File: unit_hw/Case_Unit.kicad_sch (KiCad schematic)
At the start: 15 parts, among them J1 Conn_01x02, J2 Conn_01x04, J3 RJ45, J4 Conn_01x03, Q1 2N7002, U1 SPX3819M5-L-3-3, U2 STM32G030F6Px, U3 MAX487E

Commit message: Revise unit schematic
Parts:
- removed J1: Conn_01x02, Connector_PinHeader_2.54mm:PinHeader_1x02_P2.54mm_Vertical, symbol Connector_Generic:Conn_01x02
- removed Q1: 2N7002, Package_TO_SOT_SMD:SOT-23, symbol Device:Q_NMOS_GSD
- removed U1: SPX3819M5-L-3-3, Package_TO_SOT_SMD:SOT-23-5, symbol Regulator_Linear:SPX3819M5-L-3-3
- removed U2: STM32G030F6Px, Package_SO:TSSOP-20_4.4x6.5mm_P0.65mm, symbol MCU_ST_STM32G0:STM32G030F6Px
- added C3, C4: 22u, Capacitor_SMD:C_0603_1608Metric, symbol Device:C
- added C5: 100n, Capacitor_SMD:C_0402_1005Metric, symbol Device:C
- added L1: 10u, Inductor_SMD:L_Changjiang_FNR5030S, symbol Device:L
- added R2: 100k, Resistor_SMD:R_0402_1005Metric, symbol Device:R
- added R3: 13k, Resistor_SMD:R_0402_1005Metric, symbol Device:R
- added U1: MT2492, Package_TO_SOT_SMD:SOT-23-6, symbol MT2492:MT2492
- added U2: PY32F003F18U6, Package_DFN_QFN:QFN-20-1EP_3x3mm_P0.4mm_EP1.65x1.65mm, symbol Case_symbols:PY32F003F18U6TR
- C1: value 4.7u -> 100n; footprint Capacitor_SMD:C_0402_1005Metric -> Capacitor_SMD:C_0603_1608Metric
- C2: value 10n -> 22u; footprint Capacitor_SMD:C_0402_1005Metric -> Capacitor_SMD:C_0603_1608Metric
- R1: value 4.7k -> 1; footprint Resistor_SMD:R_0402_1005Metric -> (none)
- renumbered C3 to C6, C4 to C7, J2 to J1, R3 to R4, R2 to R5
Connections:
- net MAX487_RE is gone; now on net MAX487_DE: U3.2 (~{RE})
- net +5V: now also C6.1, J1.1 (Pin_1), C3.1, C4.1, L1.2, R2.1, U2.6 (VCC); no longer R1.1
- net GND: now also J3.2, C3.2, C4.2, R3.2, U1.2 (GND), U2.21 (PAD), U2.4 (VSS)
- net MAX487_DE: now also U2.20 (PA4)
- net SERVO_OUT: now also U2.16 (PA0); no longer R1.2
- net SWCLK: now also U2.8 (PA14)
- net SWDIO: now also U2.7 (PA13)
- net UART_RX: now also U2.19 (PA3)
- net UART_TX: now also U2.18 (PA2)
- net at C2.1: now also R1.2, U1.4 (EN), U1.5 (IN)
- net VIN: now reaches J3.1
- net VIN: now also C1.1, R1.1
- removed net +3V3: C1.1, C6.1, J1.1 (Pin_1)
- new net: C5.1, U1.1 (BS)
- new net: R2.2, R3.1, U1.3 (FB)
- new net: C5.2, L1.1, U1.6 (SW)
- no-connect marks 17 -> 16
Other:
- note added: "(130k)"
- note added: "(20k)"
- note added: "Consider MP2359"
- note added: "FB ref. 0.6 V typ. (0.8 V MP2359)"
- note added: "PA0 AF13 TIM1_CH3"
- note added: "PA2 AF1 USART1_TX"
- note added: "PA3 AF1 USART1_RX"
- note added: "Set output = 5.2 V"
- note removed: "PA2 AF1 USART2_TX"
- note removed: "PA3 AF1 USART2_RX FT_ea"
- note removed: "PA7 AF5 TIM17_CH1"
- moved on the sheet: C6

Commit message: Submit for fab (Rev. 2 unit)
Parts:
- C1: footprint Capacitor_SMD:C_0603_1608Metric -> Capacitor_SMD:C_0402_1005Metric
- R1: footprint (none) -> Resistor_SMD:R_0402_1005Metric
- renumbered J3 to J2, J4 to J3
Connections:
- net GND: now also J2.3, J2.4, J2.5, J2.6
- net MAX487_DE: now also U2.17 (PA1); no longer U2.20 (PA4)
- net SERVO_OUT: now also U2.3 (PA7); no longer U2.16 (PA0)
- no-connect marks 16 -> 12
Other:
- note added: "PA7 AF2 TIM1_CH1N"
- note removed: "PA0 AF13 TIM1_CH3"
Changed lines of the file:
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@@
   (junction (at -6.35 43.815) (diameter 0) (color 0 0 0 0)
   )
+  (junction (at 4.445 109.855) (diameter 0) (color 0 0 0 0)
+  )
   (junction (at -6.35 51.435) (diameter 0) (color 0 0 0 0)
   )
   (junction (at 127.635 106.68) (diameter 0) (color 0 0 0 0)
   )
+  (junction (at 4.445 114.935) (diameter 0) (color 0 0 0 0)
+  )
   (junction (at 104.14 111.76) (diameter 0) (color 0 0 0 0)
   )
+  (junction (at 4.445 112.395) (diameter 0) (color 0 0 0 0)
+  )
   (junction (at -45.72 36.195) (diameter 0) (color 0 0 0 0)
   )
   (junction (at -17.78 36.195) (diameter 0) (color 0 0 0 0)
+  )
+  (junction (at 4.445 116.84) (diameter 0) (color 0 0 0 0)
   )
   (junction (at 6.985 116.84) (diameter 0) (color 0 0 0 0)
@@
   (no_connect (at 71.12 67.945))
   (no_connect (at 68.58 67.945))
-  (no_connect (at 52.705 55.245))
-  (no_connect (at 4.445 112.395))
-  (no_connect (at 4.445 109.855))
+  (no_connect (at 71.12 41.91))
   (no_connect (at 52.705 52.705))
   (no_connect (at 52.705 60.325))
-  (no_connect (at 4.445 107.315))
+  (no_connect (at 60.96 41.91))
   (no_connect (at 78.74 55.245))
   (no_connect (at 78.74 60.325))
   (no_connect (at 52.705 50.165))
   (no_connect (at 78.74 57.785))
-  (no_connect (at 4.445 114.935))
-  (no_connect (at 68.58 41.91))
   (no_connect (at 78.74 50.165))
+  (wire (pts (xy 4.445 114.935) (xy 4.445 116.84))
+    (stroke (width 0) (type default))
+  )
   (wire (pts (xy 50.165 56.515) (xy 52.705 56.515))
     (stroke (width 0) (type default))
@@
     (stroke (width 0) (type default))
   )
-  (wire (pts (xy 60.96 39.37) (xy 60.96 41.91))
+  (wire (pts (xy 68.58 39.37) (xy 68.58 41.91))
     (stroke (width 0) (type default))
   )
@@
     (stroke (width 0) (type default))
   )
+  (wire (pts (xy 4.445 109.855) (xy 4.445 112.395))
+    (stroke (width 0) (type default))
+  )
   (wire (pts (xy 6.35 104.775) (xy 4.445 104.775))
     (stroke (width 0) (type default))
@@
     (stroke (width 0) (type default))
   )
-  (wire (pts (xy 71.12 39.37) (xy 71.12 41.91))
+  (wire (pts (xy 50.165 55.245) (xy 52.705 55.245))
     (stroke (width 0) (type default))
   )
@@
     (stroke (width 0) (type default))
   )
+  (wire (pts (xy 4.445 107.315) (xy 4.445 109.855))
+    (stroke (width 0) (type default))
+  )
   (wire (pts (xy 51.435 67.945) (xy 60.96 67.945))
     (stroke (width 0) (type default))
@@
   )
   (wire (pts (xy 66.04 39.37) (xy 66.04 41.91))
+    (stroke (width 0) (type default))
+  )
+  (wire (pts (xy 4.445 112.395) (xy 4.445 114.935))
     (stroke (width 0) (type default))
   )
@@
     (effects (font (size 1.27 1.27) italic) (justify left bottom))
   )
-  (text "PA0 AF13 TIM1_CH3" (at 72.39 31.75 0)
-    (effects (font (size 1.27 1.27) italic) (justify left bottom))
+  (text "PA7 AF2 TIM1_CH1N" (at 50.165 52.705 0)
+    (effects (font (size 1.27 1.27) italic) (justify right bottom))
   )
   (text "(20k)" (at -4.445 49.53 0)
@@
     (effects (font (size 1.27 1.27)) (justify right bottom))
   )
-  (label "SERVO_OUT" (at 71.12 39.37 90) (fields_autoplaced)
-    (effects (font (size 1.27 1.27)) (justify left bottom))
+  (label "SERVO_OUT" (at 50.165 55.245 180) (fields_autoplaced)
+    (effects (font (size 1.27 1.27)) (justify right bottom))
   )
   (label "RS422-" (at 6.35 102.235 0) (fields_autoplaced)
     (effects (font (size 1.27 1.27)) (justify left bottom))
   )
-  (label "MAX487_DE" (at 60.96 39.37 90) (fields_autoplaced)
+  (label "MAX487_DE" (at 68.58 39.37 90) (fields_autoplaced)
     (effects (font (size 1.27 1.27)) (justify left bottom))
   )
@@
       (effects (font (size 1.27 1.27)))
     )
-    (property "Footprint" "" (at -58.42 37.973 90)
+    (property "Footprint" "Resistor_SMD:R_0402_1005Metric" (at -58.42 37.973 90)
       (effects (font (size 1.27 1.27)) hide)
     )
@@
       (effects (font (size 1.27 1.27)) (justify left))
     )
-    (property "Footprint" "Capacitor_SMD:C_0603_1608Metric" (at -67.0052 43.815 0)
+    (property "Footprint" "Capacitor_SMD:C_0402_1005Metric" (at -67.0052 43.815 0)
       (effects (font (size 1.27 1.27)) hide)
     )
@@
   (symbol (lib_id "Connector_Generic:Conn_01x03") (at -11.43 133.35 0) (unit 1)
     (in_bom yes) (on_board yes) (dnp no)
-    (property "Reference" "J4" (at -8.89 133.35 0)
+    (property "Reference" "J3" (at -8.89 133.35 0)
       (effects (font (size 1.27 1.27)) (justify left))
     )
@@
       (project "Case_Unit"
         (path "/29c85a4f-01dc-47ac-a552-a3c6d1f580bd"
-          (reference "J4") (unit 1)
+          (reference "J3") (unit 1)
         )
       )
@@
   (symbol (lib_id "Connector:RJ45") (at -5.715 112.395 0) (unit 1)
     (in_bom yes) (on_board yes) (dnp no) (fields_autoplaced)
-    (property "Reference" "J3" (at -5.715 95.25 0)
+    (property "Reference" "J2" (at -5.715 95.25 0)
       (effects (font (size 1.27 1.27)))
     )
@@
       (project "Case_Unit"
         (path "/29c85a4f-01dc-47ac-a552-a3c6d1f580bd"
-          (reference "J3") (unit 1)
-        )
-      )
+          (reference "J2") (unit 1)
+        )
+      )

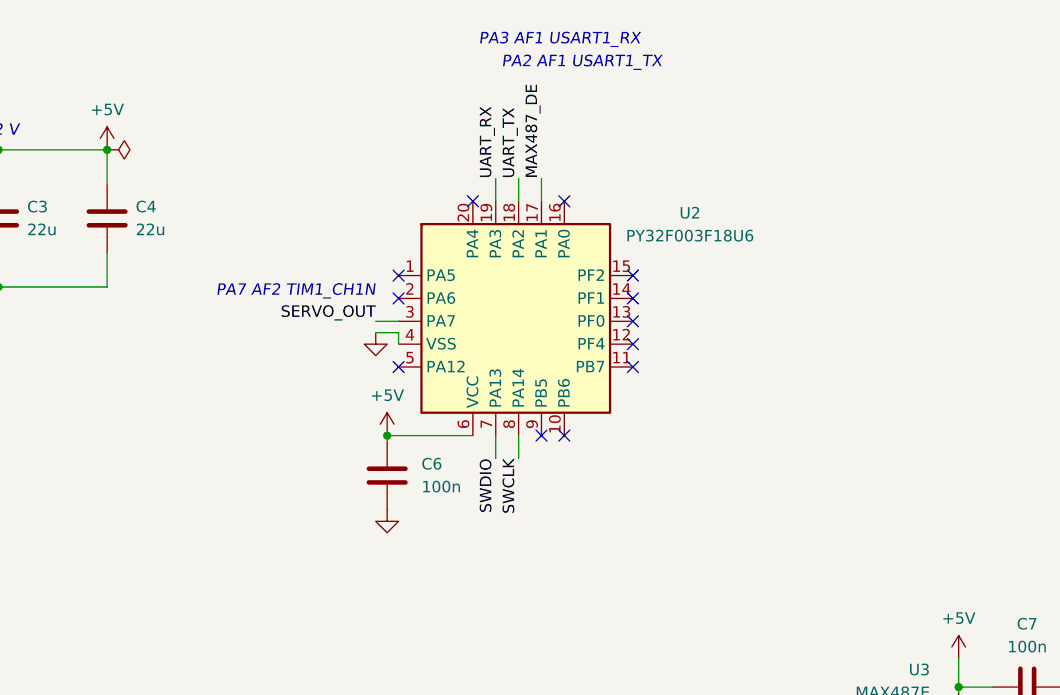
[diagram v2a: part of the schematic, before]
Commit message: Revise unit board (change PY32 model to 002B; add crystal)
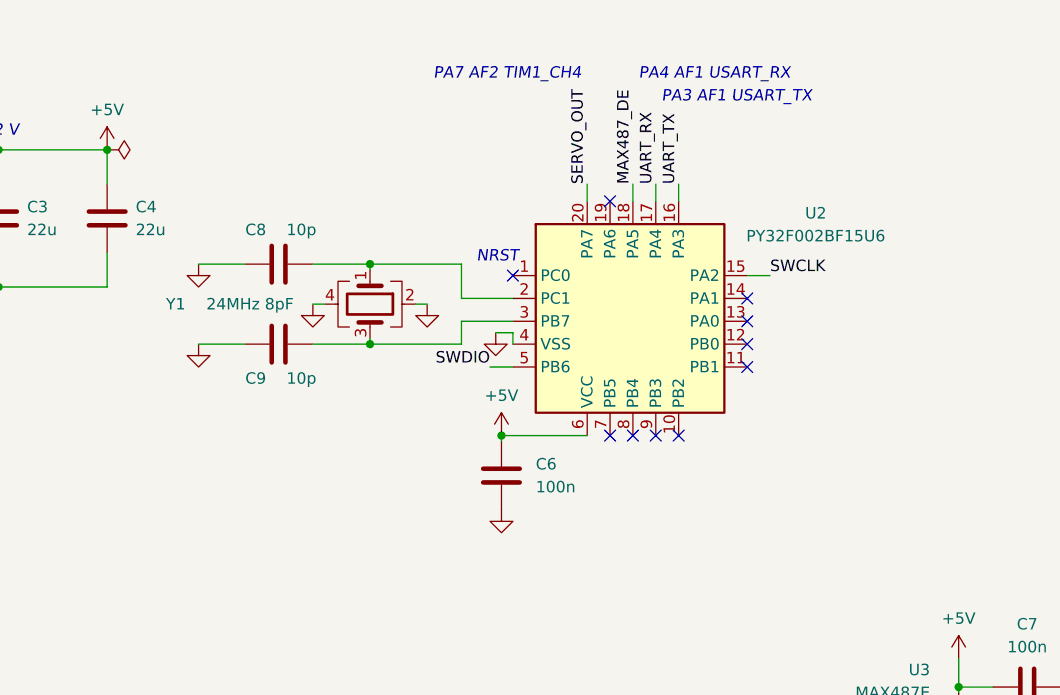
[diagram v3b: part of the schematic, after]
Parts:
- removed U2: PY32F003F18U6, Package_DFN_QFN:QFN-20-1EP_3x3mm_P0.4mm_EP1.65x1.65mm, symbol Case_symbols:PY32F003F18U6TR
- added C8, C9: 10p, Capacitor_SMD:C_0402_1005Metric, symbol Device:C
- added U2: PY32F002BF15U6, Package_DFN_QFN:QFN-20-1EP_3x3mm_P0.4mm_EP1.65x1.65mm, symbol Case_symbols:PY32F002BF15U6TR
- added Y1: 24MHz 8pF, Crystal:Crystal_SMD_2016-4Pin_2.0x1.6mm, symbol Device:Crystal_GND24
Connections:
- net +5V: now also U2.6 (VCC)
- net GND: now also C8.1, C9.1, U2.21 (PAD), U2.4 (VSS), Y1.2, Y1.4
- net MAX487_DE: now also U2.18 (PA5)
- net SERVO_OUT: now also U2.20 (PA7)
- net SWCLK: now also U2.15 (PA2)
- net SWDIO: now also U2.5 (PB6)
- net UART_RX: now also U2.17 (PA4)
- net UART_TX: now also U2.16 (PA3)
- new net: C8.2, U2.2 (PC1), Y1.1
- new net: C9.2, U2.3 (PB7), Y1.3
- no-connect marks 12 -> 10
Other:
- note added: "NRST"
- note added: "PA3 AF1 USART_TX"
- note added: "PA4 AF1 USART_RX"
- note added: "PA7 AF2 TIM1_CH4"
- note removed: "PA2 AF1 USART1_TX"
- note removed: "PA3 AF1 USART1_RX"
- note removed: "PA7 AF2 TIM1_CH1N"
- moved on the sheet: C6

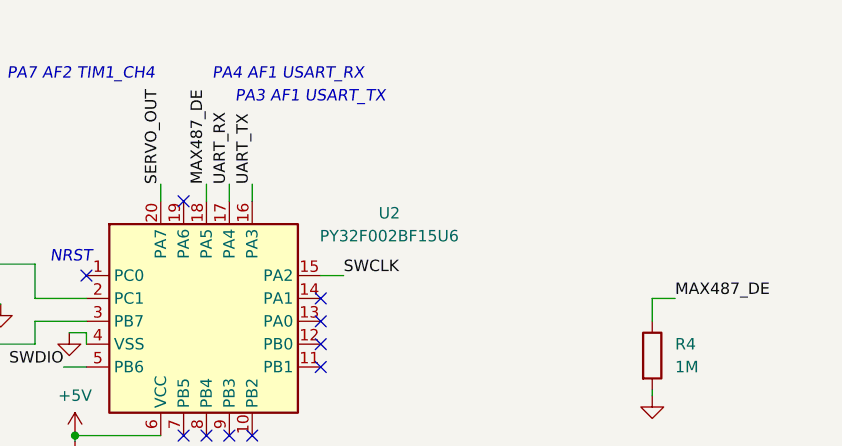
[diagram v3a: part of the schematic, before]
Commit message: Finish unit redesign; submit for fab (Rev. 2 unit)
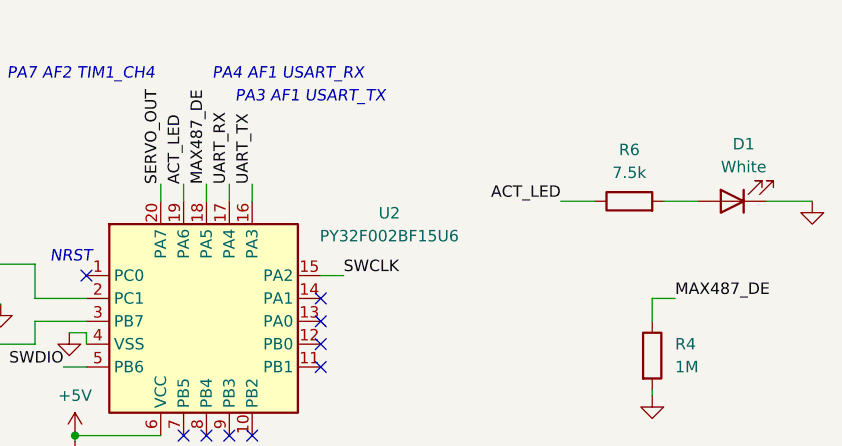
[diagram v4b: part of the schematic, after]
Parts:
- added D1: White, LED_SMD:LED_0603_1608Metric, symbol Device:LED
- added R6: 7.5k, Resistor_SMD:R_0402_1005Metric, symbol Device:R
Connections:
- net GND: now also D1.1 (K)
- net ACT_LED: now reaches U2.19 (PA6)
- net ACT_LED: now also R6.1
- new net: D1.2 (A), R6.2
- no-connect marks 10 -> 9
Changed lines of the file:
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@@
   (no_connect (at 83.82 67.945))
   (no_connect (at 81.28 67.945))
-  (no_connect (at 76.2 41.91))
   (no_connect (at 91.44 57.785))
   (no_connect (at 76.2 67.945))
@@
     (stroke (width 0) (type default))
   )
+  (wire (pts (xy 118.11 41.91) (xy 121.92 41.91))
+    (stroke (width 0) (type default))
+  )
   (wire (pts (xy 130.175 95.885) (xy 126.365 95.885))
     (stroke (width 0) (type default))
@@
     (stroke (width 0) (type default))
   )
+  (wire (pts (xy 76.2 40.005) (xy 76.2 41.91))
+    (stroke (width 0) (type default))
+  )
   (wire (pts (xy 6.35 104.775) (xy 4.445 104.775))
     (stroke (width 0) (type default))
@@
     (stroke (width 0) (type default))
   )
+  (wire (pts (xy 140.97 41.91) (xy 146.05 41.91))
+    (stroke (width 0) (type default))
+  )
   (wire (pts (xy 102.87 114.3) (xy 104.775 114.3))
     (stroke (width 0) (type default))
@@
   )
   (wire (pts (xy 4.445 120.015) (xy 13.335 120.015))
+    (stroke (width 0) (type default))
+  )
+  (wire (pts (xy 133.35 41.91) (xy 129.54 41.91))
     (stroke (width 0) (type default))
   )
@@
     (effects (font (size 1.27 1.27)) (justify right bottom))
   )
+  (label "ACT_LED" (at 76.2 40.005 90) (fields_autoplaced)
+    (effects (font (size 1.27 1.27)) (justify left bottom))
+  )
   (label "RS422+" (at 6.35 104.775 0) (fields_autoplaced)
     (effects (font (size 1.27 1.27)) (justify left bottom))
@@
   (label "RS422-" (at 6.35 102.235 0) (fields_autoplaced)
     (effects (font (size 1.27 1.27)) (justify left bottom))
+  )
+  (label "ACT_LED" (at 118.11 41.91 180) (fields_autoplaced)
+    (effects (font (size 1.27 1.27)) (justify right bottom))
   )
   (label "MAX487_DE" (at 130.81 52.705 0) (fields_autoplaced)
@@
     )
   )
+  (symbol (lib_id "Device:LED") (at 137.16 41.91 180) (unit 1)
+    (in_bom yes) (on_board yes) (dnp no)
+    (property "Reference" "D1" (at 138.43 35.56 0)
+      (effects (font (size 1.27 1.27)))
+    )
+    (property "Value" "White" (at 138.43 38.1 0)
+      (effects (font (size 1.27 1.27)))
+    )
+    (property "Footprint" "LED_SMD:LED_0603_1608Metric" (at 137.16 41.91 0)
+      (effects (font (size 1.27 1.27)) hide)
+    )
+    (property "Datasheet" "~" (at 137.16 41.91 0)
+      (effects (font (size 1.27 1.27)) hide)
+    )
+    (pin "1")
+    (pin "2")
+    (instances
+      (project "Case_Unit"
+        (path "/29c85a4f-01dc-47ac-a552-a3c6d1f580bd"
+          (reference "D1") (unit 1)
+        )
+      )
+    )
+  )
   (symbol (lib_id "power:GND") (at 63.5 56.515 0) (unit 1)
     (in_bom yes) (on_board yes) (dnp no) (fields_autoplaced)
@@
         (path "/29c85a4f-01dc-47ac-a552-a3c6d1f580bd"
           (reference "R1") (unit 1)
+        )
+      )
+    )
+  )
+  (symbol (lib_id "Device:R") (at 125.73 41.91 90) (unit 1)
+    (in_bom yes) (on_board yes) (dnp no)
+    (property "Reference" "R6" (at 125.73 36.195 90)
+      (effects (font (size 1.27 1.27)))
+    )
+    (property "Value" "7.5k" (at 125.73 38.735 90)
+      (effects (font (size 1.27 1.27)))
+    )
+    (property "Footprint" "Resistor_SMD:R_0402_1005Metric" (at 125.73 43.688 90)
+      (effects (font (size 1.27 1.27)) hide)
+    )
+    (property "Datasheet" "~" (at 125.73 41.91 0)
+      (effects (font (size 1.27 1.27)) hide)
+    )
+    (pin "2")
+    (pin "1")
+    (instances
+      (project "Case_Unit"
+        (path "/29c85a4f-01dc-47ac-a552-a3c6d1f580bd"
+          (reference "R6") (unit 1)
         )
       )
@@
         )
       )
+    )
+  )
+  (symbol (lib_id "power:GND") (at 146.05 41.91 0) (unit 1)
+    (in_bom yes) (on_board yes) (dnp no) (fields_autoplaced)
+    (property "Reference" "#PWR024" (at 146.05 48.26 0)
+      (effects (font (size 1.27 1.27)) hide)
+    )
+    (property "Value" "GND" (at 146.05 46.355 0)
+      (effects (font (size 1.27 1.27)) hide)
+    )
+    (property "Footprint" "" (at 146.05 41.91 0)
+      (effects (font (size 1.27 1.27)) hide)
+    )
+    (property "Datasheet" "" (at 146.05 41.91 0)
+      (effects (font (size 1.27 1.27)) hide)
+    )
+    (pin "1")
+    (instances
+      (project "Case_Unit"
+        (path "/29c85a4f-01dc-47ac-a552-a3c6d1f580bd"
+          (reference "#PWR024") (unit 1)
+        )
+      )
